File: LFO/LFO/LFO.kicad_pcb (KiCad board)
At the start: 2 copper layers, 84 parts, among them Q1 NJFET, Q2 NJFET, Q3 2N3904, Q4 2N3904, Q5 2N3906, Q6 2N3904, U1 LM13700, U2 TL082, U3 TL082, U4 TL072, U5 TL082, U6 TL082

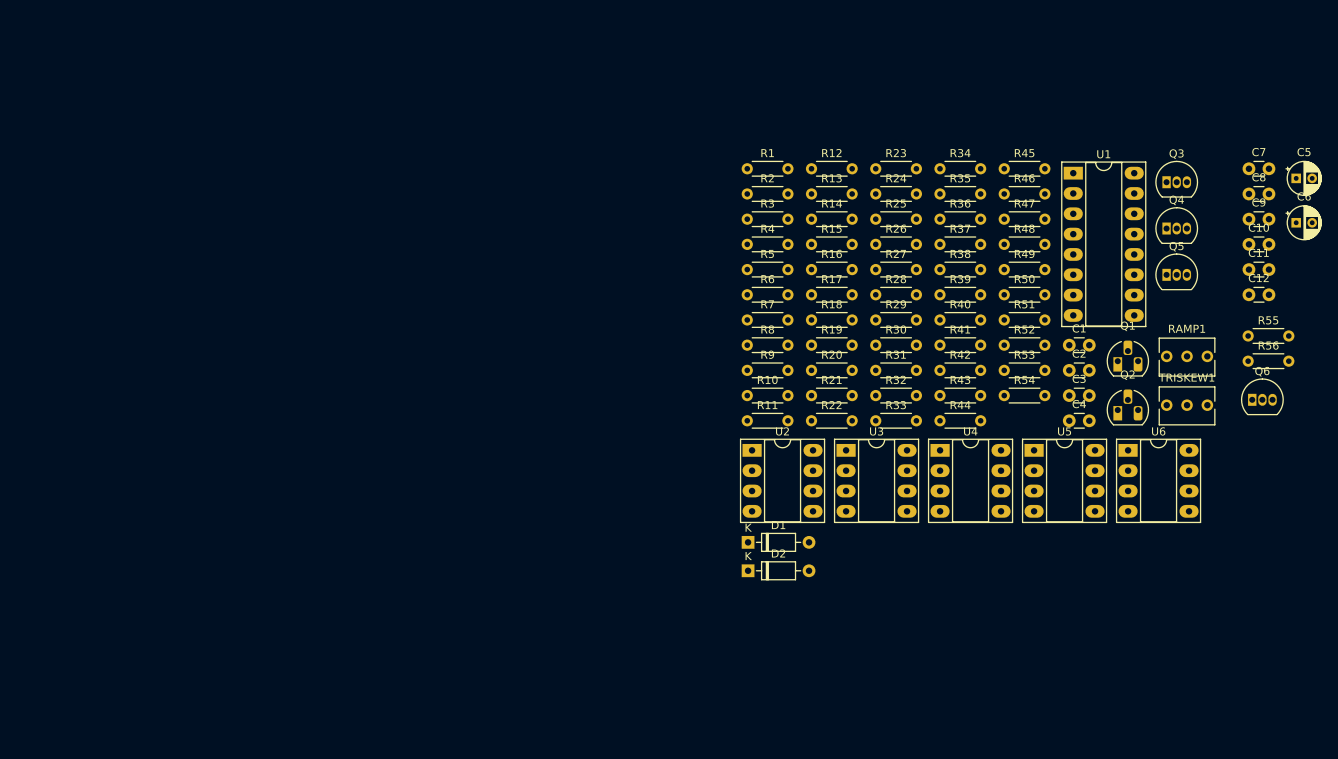
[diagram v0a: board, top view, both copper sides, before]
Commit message: added missing connectors
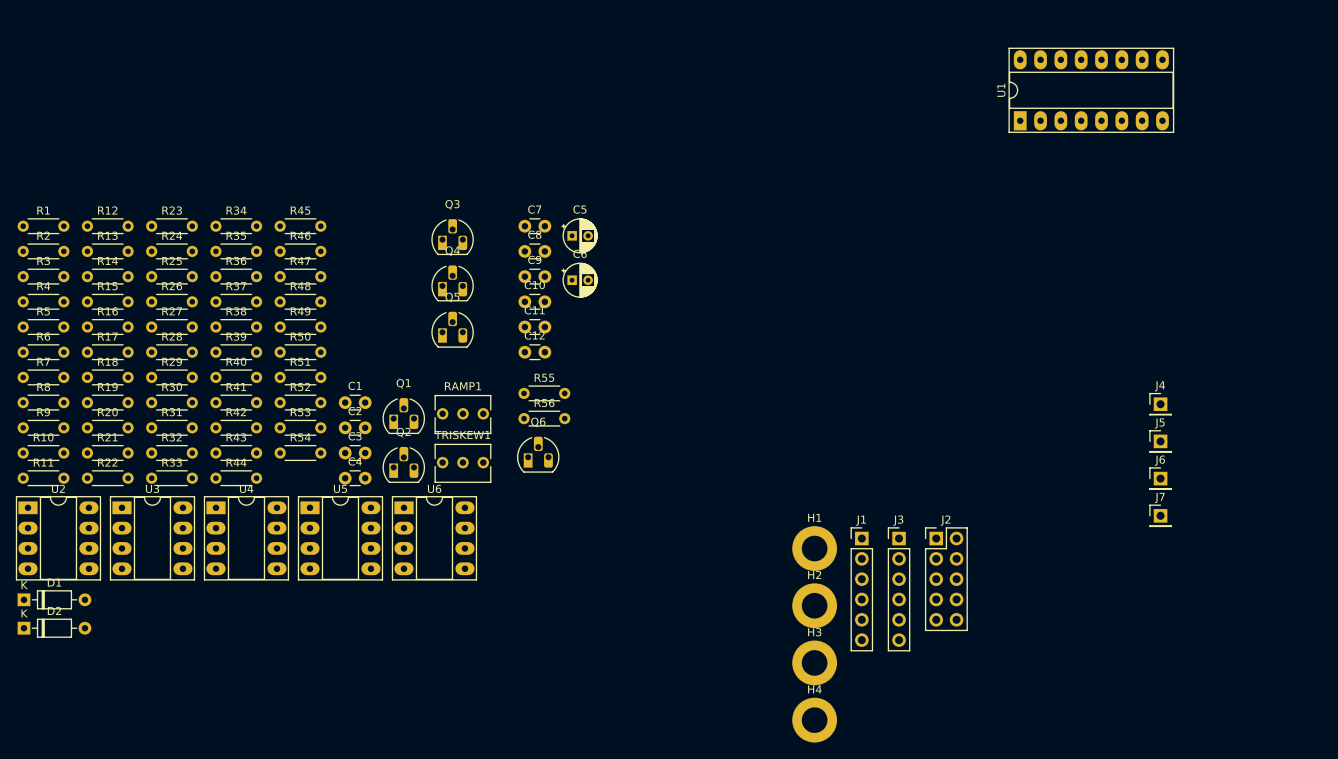
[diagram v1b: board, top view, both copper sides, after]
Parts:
- added H1: MountingHole_Pad, MountingHole:MountingHole_3.2mm_M3_DIN965_Pad, F.Cu at (124.8, 119.6)
- added H2: MountingHole_Pad, MountingHole:MountingHole_3.2mm_M3_DIN965_Pad, F.Cu at (124.8, 126.7)
- added H3: MountingHole_Pad, MountingHole:MountingHole_3.2mm_M3_DIN965_Pad, F.Cu at (124.8, 133.9)
- added H4: MountingHole_Pad, MountingHole:MountingHole_3.2mm_M3_DIN965_Pad, F.Cu at (124.8, 141.0)
- added J1: Conn_01x06, Connector_PinHeader_2.54mm:PinHeader_1x06_P2.54mm_Vertical, F.Cu at (130.7, 118.3)
- added J2: Conn_02x05_Odd_Even, Connector_PinHeader_2.54mm:PinHeader_2x05_P2.54mm_Vertical, F.Cu at (140.0, 118.3)
- added J3: Conn_01x06, Connector_PinHeader_2.54mm:PinHeader_1x06_P2.54mm_Vertical, F.Cu at (135.3, 118.3)
- added J4: Conn_01x01, Connector_PinHeader_2.54mm:PinHeader_1x01_P2.54mm_Vertical, F.Cu at (168.0, 101.5)
- added J5: Conn_01x01, Connector_PinHeader_2.54mm:PinHeader_1x01_P2.54mm_Vertical, F.Cu at (168.0, 106.2)
- added J6: Conn_01x01, Connector_PinHeader_2.54mm:PinHeader_1x01_P2.54mm_Vertical, F.Cu at (168.0, 110.8)
- added J7: Conn_01x01, Connector_PinHeader_2.54mm:PinHeader_1x01_P2.54mm_Vertical, F.Cu at (168.0, 115.5)
- Q3, Q4, Q5, Q6: footprint Package_TO_SOT_THT:TO-92_Inline -> Package_TO_SOT_THT:TO-92_HandSolder
- moved C1 90.8 mm to (66.1, 101.3)
- moved C10 90.8 mm to (88.5, 88.8)
- moved C11 90.8 mm to (88.5, 91.9)
- moved C12 90.8 mm to (88.5, 95.0)
- moved C2 90.8 mm to (66.1, 104.5)
- moved C3 90.8 mm to (66.1, 107.7)
- moved C4 90.8 mm to (66.1, 110.8)
- moved C5 90.8 mm to (94.4, 80.5)
- moved C6 90.8 mm to (94.4, 86.0)
- moved C7 90.8 mm to (88.5, 79.3)
- moved C8 90.8 mm to (88.5, 82.5)
- moved C9 90.8 mm to (88.5, 85.6)
- moved Q1 90.8 mm to (72.1, 103.3)
- moved Q2 90.8 mm to (72.1, 109.5)
- moved Q3 90.8 mm to (78.2, 81.0)
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
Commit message: most of PCB done
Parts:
- removed H3, H4: MountingHole_Pad, MountingHole:MountingHole_3.2mm_M3_DIN965_Pad
- C10, C11, C12, C2, C3, C4, C7, C8, C9: footprint Capacitor_THT:C_Disc_D3.0mm_W1.6mm_P2.50mm -> Capacitor_SMD:C_0201_0603Metric
- D1, D2: footprint Diode_THT:D_DO-35_SOD27_P7.62mm_Horizontal -> Diode_SMD:D_SOD-123
- J1: footprint Connector_PinHeader_2.54mm:PinHeader_1x06_P2.54mm_Vertical -> Connector_PinHeader_2.54mm:PinHeader_1x07_P2.54mm_Vertical
- R1, R10, R11, R12, R13, R14, R15, R16, R17, R18, R19, R2, R20, R21, R22, R23, R24, R25, R26, R27, R28, R29, R3, R30, R31, R32, R33, R34, R35, R36, R37, R38, R39, R4, R40, R41, R42, R43, R44, R45, R46, R48, R49, R5, R50, R51, R52, R53, R54, R55, R56, R6, R7, R8, R9: footprint Resistor_THT:R_Axial_DIN0204_L3.6mm_D1.6mm_P5.08mm_Horizontal -> Resistor_SMD:R_0805_2012Metric
- R47: value 10K -> 4.7K; footprint Resistor_THT:R_Axial_DIN0204_L3.6mm_D1.6mm_P5.08mm_Horizontal -> Resistor_SMD:R_0805_2012Metric
- U1: footprint Package_DIP:DIP-16_W7.62mm_Socket_LongPads -> Package_SO:SOP-16_4.4x10.4mm_P1.27mm
- U2, U3, U4, U5, U6: footprint Package_DIP:DIP-8_W7.62mm_Socket_LongPads -> Package_SO:SOP-8_3.9x4.9mm_P1.27mm
- moved U2 138.9 mm to (154.3, 60.2), turned to 90 degrees
- moved R8 137.2 mm to (159.0, 68.5), turned to -90 degrees
- moved R5 137.0 mm to (157.9, 55.4), turned to 180 degrees
- moved R7 135.4 mm to (154.3, 55.4), turned to 180 degrees
- moved D1 133.5 mm to (147.2, 70.1), turned to 180 degrees
- moved D2 132.9 mm to (147.2, 75.2)
- moved R6 127.7 mm to (150.9, 69.2), turned to 90 degrees
- moved U3 124.7 mm to (155.2, 71.4), turned to 90 degrees
- moved R9 122.0 mm to (142.9, 70.1)
- moved R10 121.5 mm to (142.9, 75.2)
- moved R26 120.9 mm to (158.9, 58.3), turned to -90 degrees
- moved R25 116.5 mm to (158.1, 77.2), turned to 180 degrees
- moved R30 115.3 mm to (154.6, 77.2), turned to 180 degrees
- moved R1 113.9 mm to (139.2, 67.8)
- moved R27 112.2 mm to (149.6, 60.3), turned to -90 degrees
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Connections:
- J1 pad 1: CFL -> CFH
- J1 pad 2: FFV -> CFL
- J1 pad 3: CFV -> FFV
- J1 pad 4: CV3 -> CFV
- J1 pad 5: CV2 -> CV3
- J1 pad 6: CV1 -> CV2
- R17 pad 1: Net-(R17-Pad1) -> CFH
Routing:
- net GND: track 0.00 -> 62.6 mm, vias 0 -> 9
- net +12V: track 0.00 -> 62.0 mm
- net Net-(Q2-S): track 0.00 -> 47.5 mm
- net -12V: track 0.00 -> 23.7 mm
- net Net-(U4A--): track 0.00 -> 19.0 mm
- net Net-(R24-Pad2): track 0.00 -> 16.2 mm
- net Net-(D1-K): track 0.00 -> 15.9 mm
- net Net-(U2A--): track 0.00 -> 14.3 mm
- net Net-(U6A--): track 0.00 -> 12.9 mm
- net Net-(Q3-C): track 0.00 -> 12.4 mm
- net ZZ: track 0.00 -> 10.2 mm, vias 0 -> 2
- net Net-(R50-Pad2): track 0.00 -> 9.63 mm
- net Net-(U3B--): track 0.00 -> 9.52 mm
- net Net-(Q3-E): track 0.00 -> 9.50 mm
- net Net-(U5B--): track 0.00 -> 8.67 mm
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- added copper zone on B.Cu, net GND
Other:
- board outline added: 49.8 x 44.3 mm
- board text added: "LFO - V1 Music From Outer Space"
- board text added: "RAMP"
- board text added: "TRISKEW"

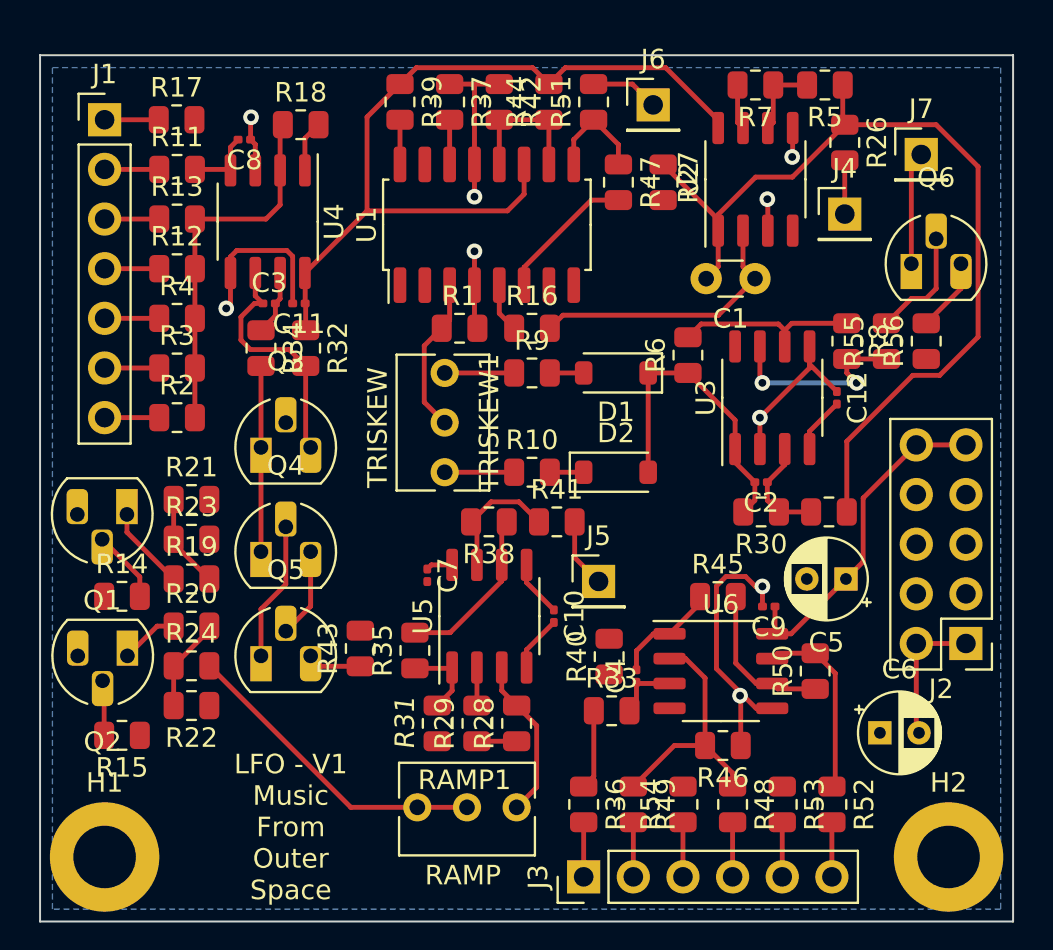
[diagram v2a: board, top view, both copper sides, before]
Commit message: corrected capacitor sizes in bom
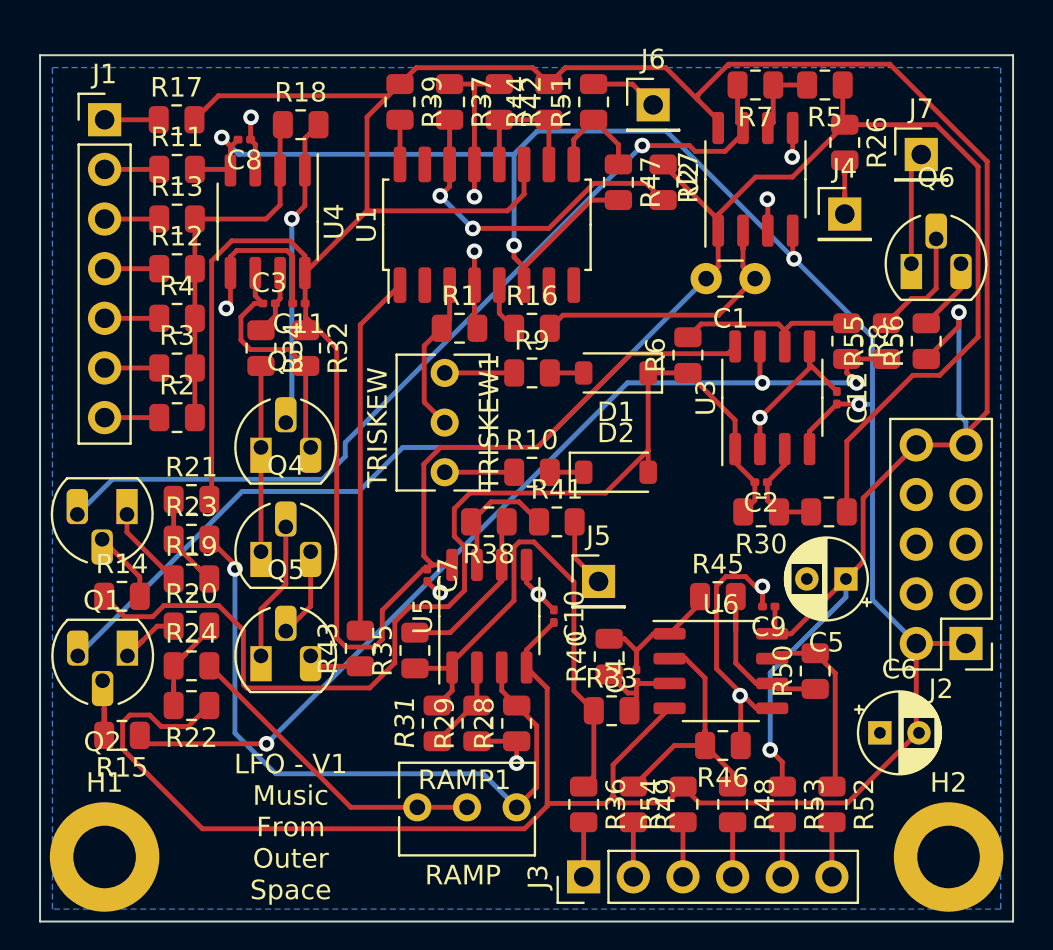
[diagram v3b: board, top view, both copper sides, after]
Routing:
- net +12V: track 62.0 -> 195.0 mm, vias 0 -> 2
- net -12V: track 23.7 -> 154.0 mm, vias 0 -> 4
- net Net-(Q1-S): track 2.32 -> 45.4 mm, vias 0 -> 1
- net Net-(D1-K): track 15.9 -> 57.2 mm
- net Net-(Q2-S): track 47.5 -> 87.7 mm
- net ZZ: track 10.2 -> 49.9 mm, vias 2 -> 3
- net Net-(U5A-+): track 8.32 -> 34.8 mm, vias 0 -> 1
- net Net-(R43-Pad2): track 0.00 -> 18.5 mm
- net Net-(R31-Pad2): track 8.28 -> 26.8 mm
- net Net-(U1A-+): track 2.29 -> 17.5 mm, vias 0 -> 2
- net Net-(Q3-B): track 2.62 -> 15.9 mm, vias 0 -> 1
- net GND: track 62.6 -> 67.7 mm, vias 9 -> 12
- net Net-(U5A--): track 1.95 -> 4.81 mm
- net Net-(C4-Pad2): track 5.58 -> 7.88 mm
- net Net-(R19-Pad2): track 4.82 -> 6.87 mm
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
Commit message: minor fixes after first build
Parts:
- added J3: Conn_01x03, Connector_PinHeader_2.54mm:PinHeader_1x03_P2.54mm_Vertical, F.Cu at (127.8, 95.9)
- renumbered J3 to J2, J2 to J4, J7 to LEDA1, J5 to SAW1, J6 to SIN1, J4 to TRI1
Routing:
- net +12V: track 195.0 -> 254.1 mm
- net -12V: track 154.0 -> 156.4 mm
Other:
- board text added: "+12V"
- board text added: "-12V"

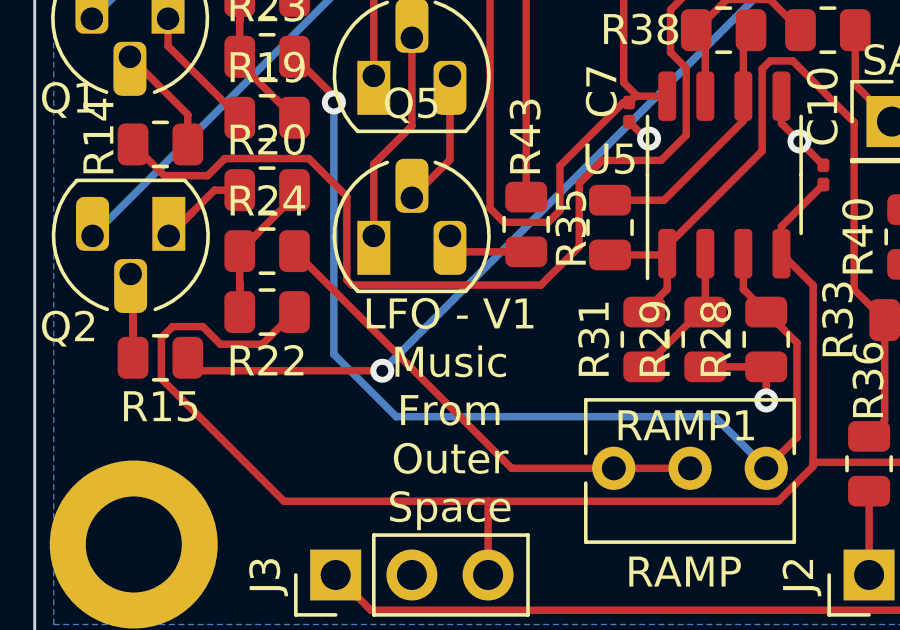
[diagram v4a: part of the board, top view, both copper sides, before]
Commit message: minor cleanup of silkscreen
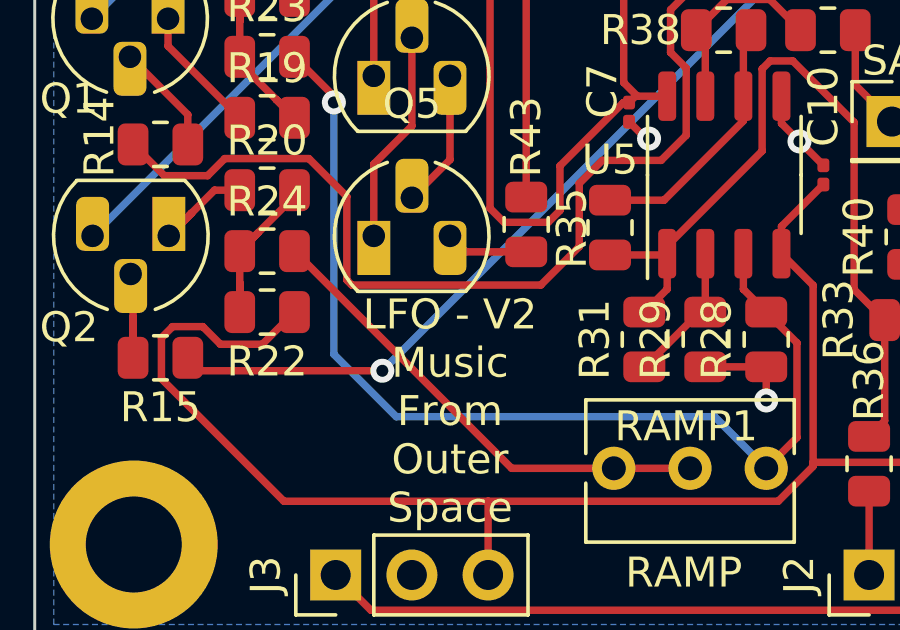
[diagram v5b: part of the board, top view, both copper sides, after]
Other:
- board text added: "LFO - V2 Music From Outer Space"
- board text removed: "LFO - V1 Music From Outer Space"
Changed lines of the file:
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@@
     (effects (font (size 1 1) (thickness 0.15)))
   )
-  (gr_text "LFO - V1\nMusic\nFrom\nOuter\nSpace" (at 131.572 90.424) (layer "F.SilkS")
+  (gr_text "LFO - V2\nMusic\nFrom\nOuter\nSpace" (at 131.572 90.424) (layer "F.SilkS")
     (effects (font (size 1 1) (thickness 0.15)))
   )
